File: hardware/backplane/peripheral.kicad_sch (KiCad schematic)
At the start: 1 part

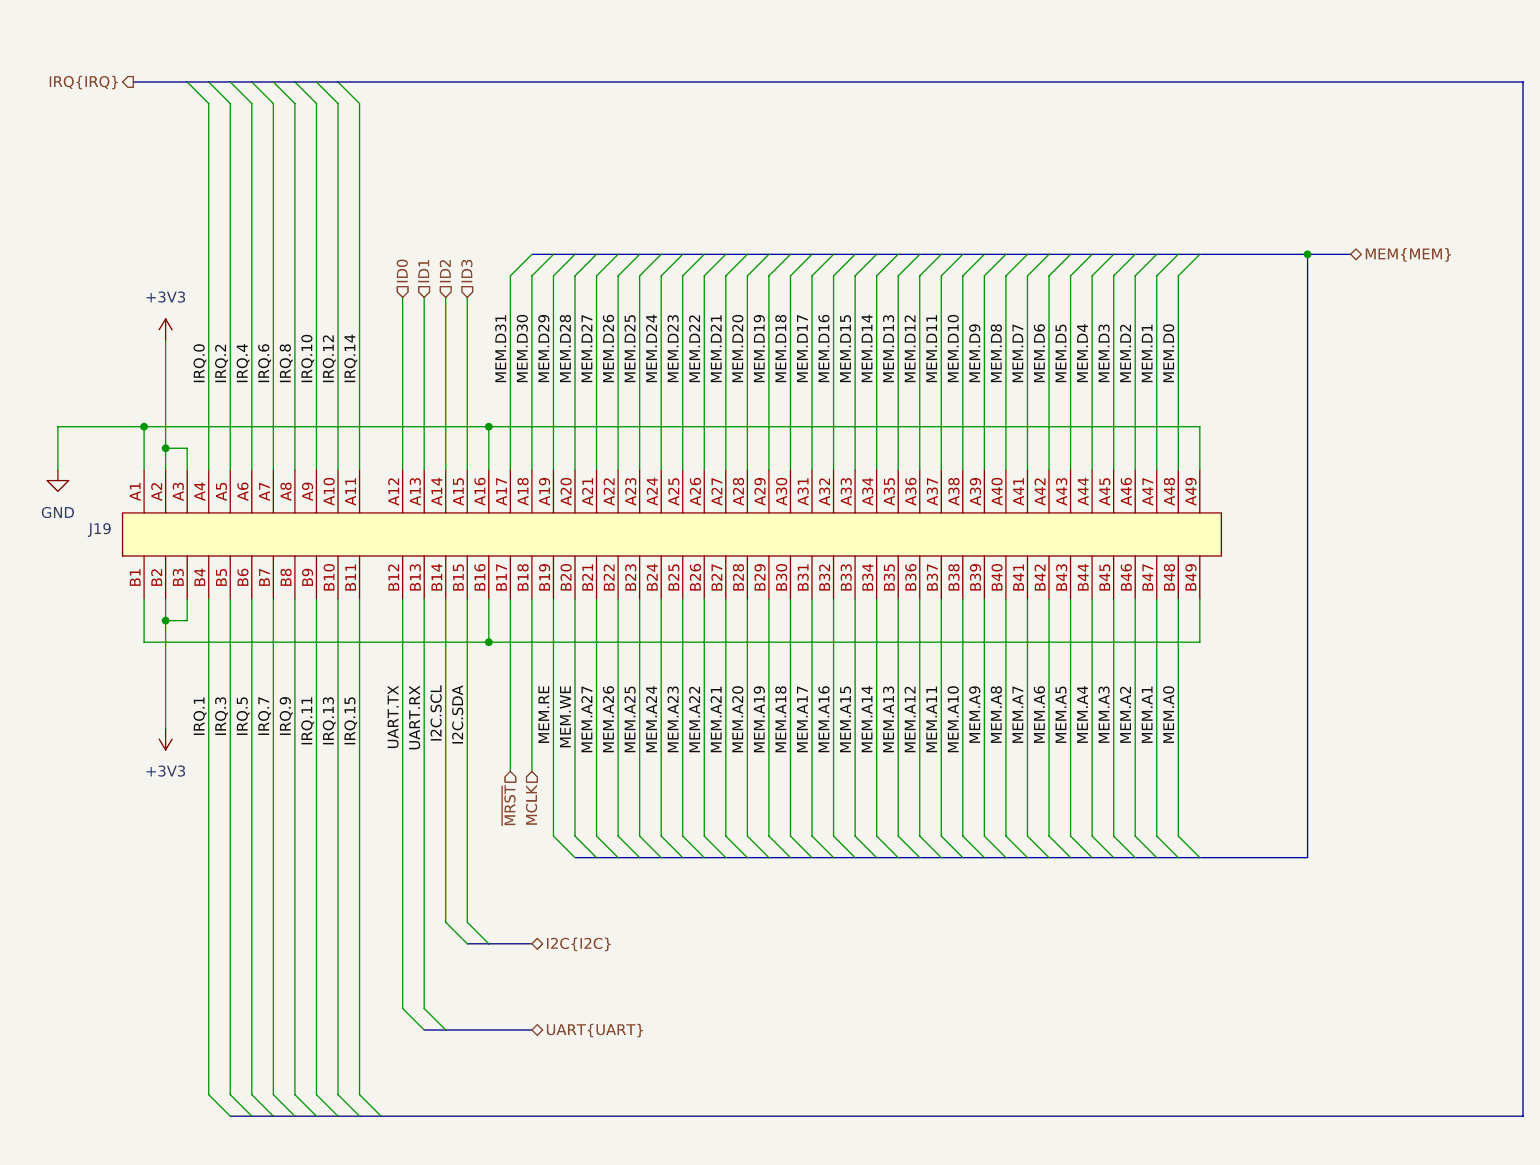
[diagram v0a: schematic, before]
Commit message: feat: Re-add peripheral MCLK, add to memory lines (#3)
Need MCLK to maintain peripheral synchronization.  Add missing memory
access size and latch lines.
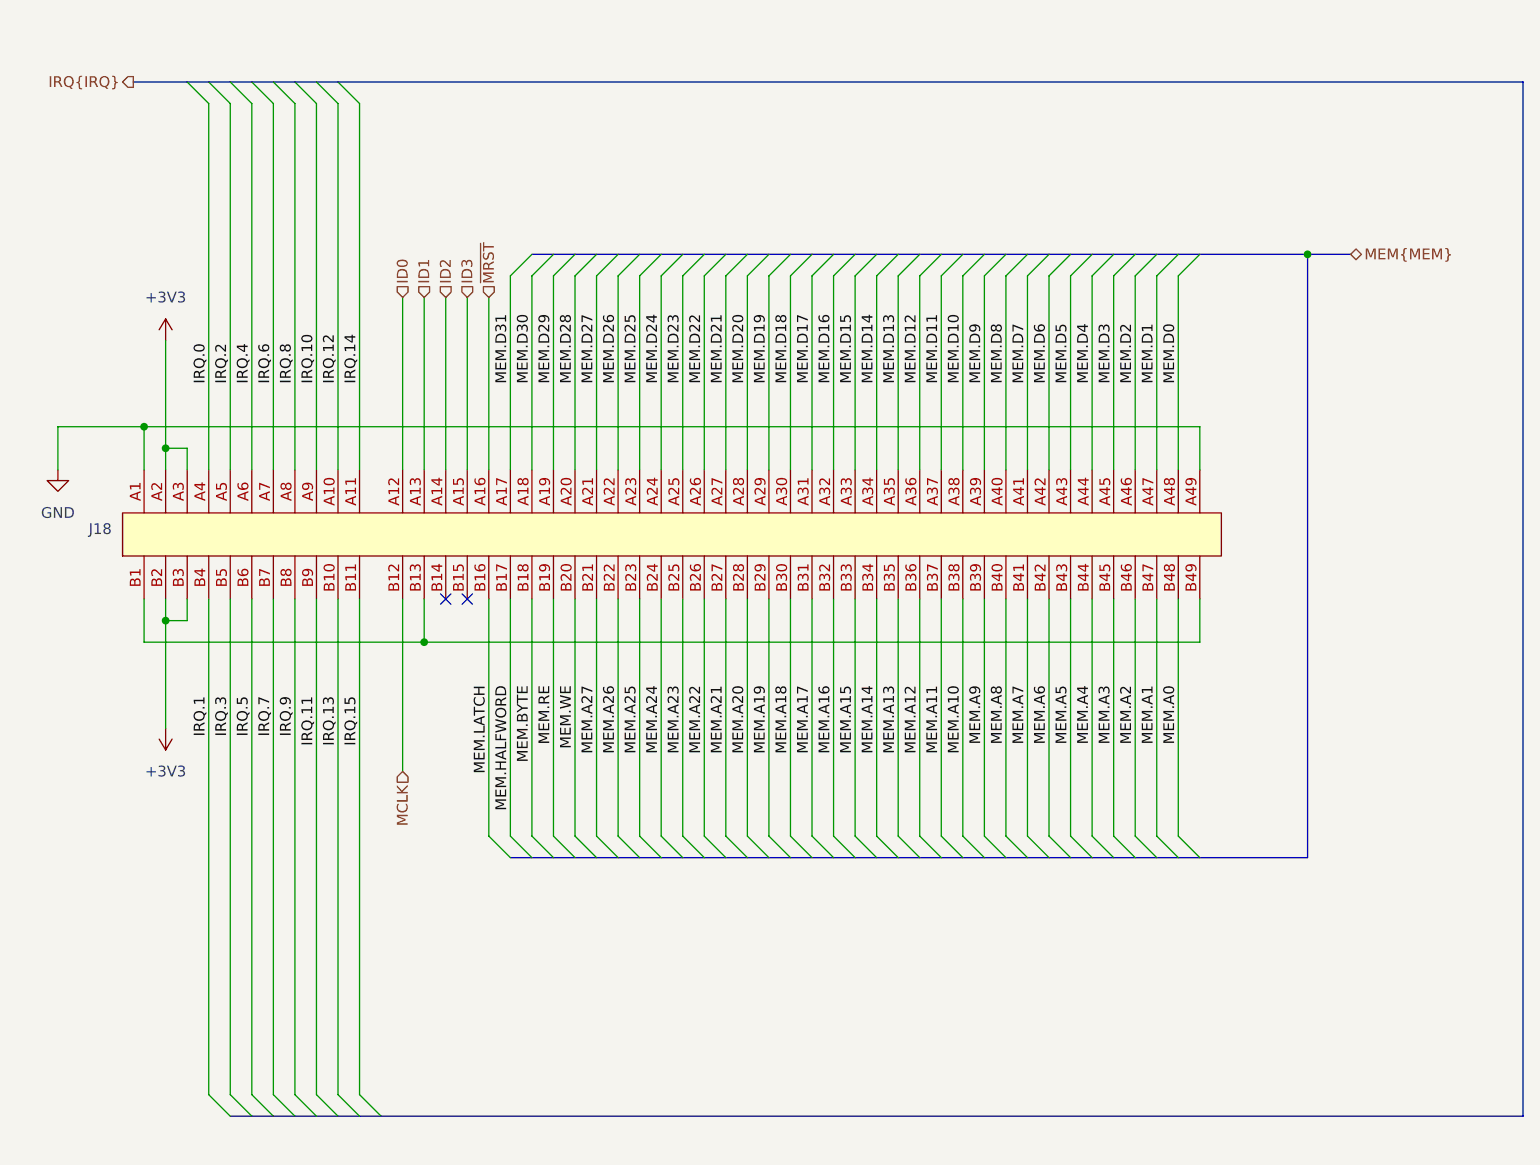
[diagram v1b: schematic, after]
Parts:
- renumbered J19 to J18
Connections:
- net UART.RX is gone; now on an unnamed net: J18.B13
- net UART.TX is gone; now on net MCLK: J18.B12
- net GND: no longer J18.A16
- net MCLK: no longer J18.B18
- net ~{MRST}: now also J18.A16; no longer J18.B17
- net at J18.B1, J18.B49: no longer J18.B16
- net I2C.SCL: no longer names the net of J18.B14
- net I2C.SDA: no longer names the net of J18.B15
- new net MEM.BYTE: J18.B18
- new net MEM.HALFWORD: J18.B17
- new net MEM.LATCH: J18.B16
- no-connect marks 0 -> 2

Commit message: feat: Assign footprints, add testpoints
 * Verify all footprints are assigned.
 * Create testpoints for key signals.
 * Reorganize component libraries.
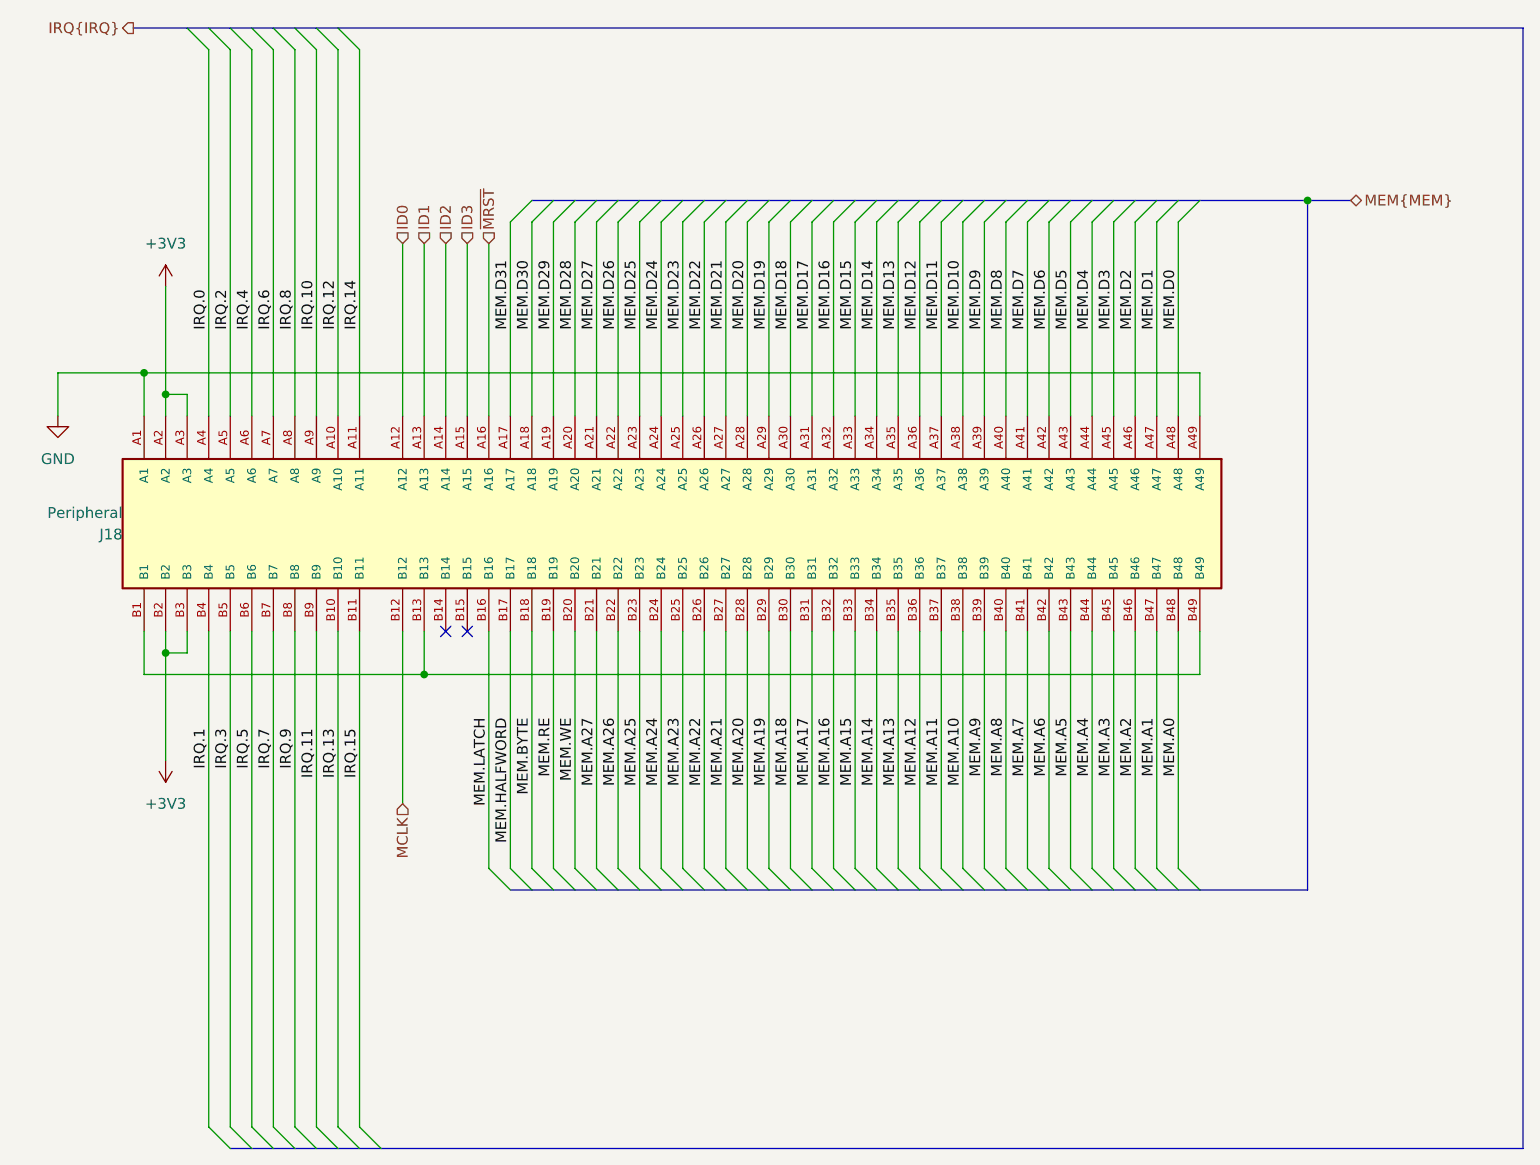
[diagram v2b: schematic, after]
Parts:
- removed J18: ~, symbol Connector_PCIe:PCIe_x8
- added J18: Peripheral, 10018783_10202TLF:AMPHENOL_10018783-10202TLF, symbol 10018783-10202TLF:10018783-10202TLF
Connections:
- net +3V3: now also J18.A2, J18.A3, J18.B2, J18.B3
- net GND: now also J18.A1, J18.A49
- net ID0: now also J18.A12
- net ID1: now also J18.A13
- net ID2: now also J18.A14
- net ID3: now also J18.A15
- net IRQ.0: now also J18.A4
- net IRQ.1: now also J18.B4
- net IRQ.10: now also J18.A9
- net IRQ.11: now also J18.B9
- net IRQ.12: now also J18.A10
- net IRQ.13: now also J18.B10
- net IRQ.14: now also J18.A11
- net IRQ.15: now also J18.B11
- net IRQ.2: now also J18.A5
- net IRQ.3: now also J18.B5
- net IRQ.4: now also J18.A6
- net IRQ.5: now also J18.B6
- net IRQ.6: now also J18.A7
- net IRQ.7: now also J18.B7
- net IRQ.8: now also J18.A8
- net IRQ.9: now also J18.B8
- net MCLK: now also J18.B12
- net MEM.A0: now also J18.B48
- net MEM.A1: now also J18.B47
- net MEM.A10: now also J18.B38
- net MEM.A11: now also J18.B37
- net MEM.A12: now also J18.B36
- net MEM.A13: now also J18.B35
- net MEM.A14: now also J18.B34
- net MEM.A15: now also J18.B33
- net MEM.A16: now also J18.B32
- net MEM.A17: now also J18.B31
- net MEM.A18: now also J18.B30
- net MEM.A19: now also J18.B29
- net MEM.A2: now also J18.B46
- net MEM.A20: now also J18.B28
- net MEM.A21: now also J18.B27
- net MEM.A22: now also J18.B26
- net MEM.A23: now also J18.B25
- net MEM.A24: now also J18.B24
- net MEM.A25: now also J18.B23
- net MEM.A26: now also J18.B22
- net MEM.A27: now also J18.B21
- net MEM.A3: now also J18.B45
- net MEM.A4: now also J18.B44
- net MEM.A5: now also J18.B43
- net MEM.A6: now also J18.B42
- net MEM.A7: now also J18.B41
- net MEM.A8: now also J18.B40
- net MEM.A9: now also J18.B39
- net MEM.BYTE: now also J18.B18
- net MEM.D0: now also J18.A48
- net MEM.D1: now also J18.A47
- net MEM.D10: now also J18.A38
- net MEM.D11: now also J18.A37
- net MEM.D12: now also J18.A36
- net MEM.D13: now also J18.A35
- net MEM.D14: now also J18.A34
- net MEM.D15: now also J18.A33
- net MEM.D16: now also J18.A32
- net MEM.D17: now also J18.A31
- net MEM.D18: now also J18.A30
- net MEM.D19: now also J18.A29
- net MEM.D2: now also J18.A46
- net MEM.D20: now also J18.A28
- net MEM.D21: now also J18.A27
- net MEM.D22: now also J18.A26
- net MEM.D23: now also J18.A25
- net MEM.D24: now also J18.A24
- net MEM.D25: now also J18.A23
- net MEM.D26: now also J18.A22
- net MEM.D27: now also J18.A21
- net MEM.D28: now also J18.A20
- net MEM.D29: now also J18.A19
- net MEM.D3: now also J18.A45
- net MEM.D30: now also J18.A18
- net MEM.D31: now also J18.A17
- net MEM.D4: now also J18.A44
- net MEM.D5: now also J18.A43
- net MEM.D6: now also J18.A42
- net MEM.D7: now also J18.A41
- net MEM.D8: now also J18.A40
- net MEM.D9: now also J18.A39
- net MEM.HALFWORD: now also J18.B17
- net MEM.LATCH: now also J18.B16
- net MEM.RE: now also J18.B19
- net MEM.WE: now also J18.B20
- net ~{MRST}: now also J18.A16
- new net: J18.B1, J18.B13, J18.B49

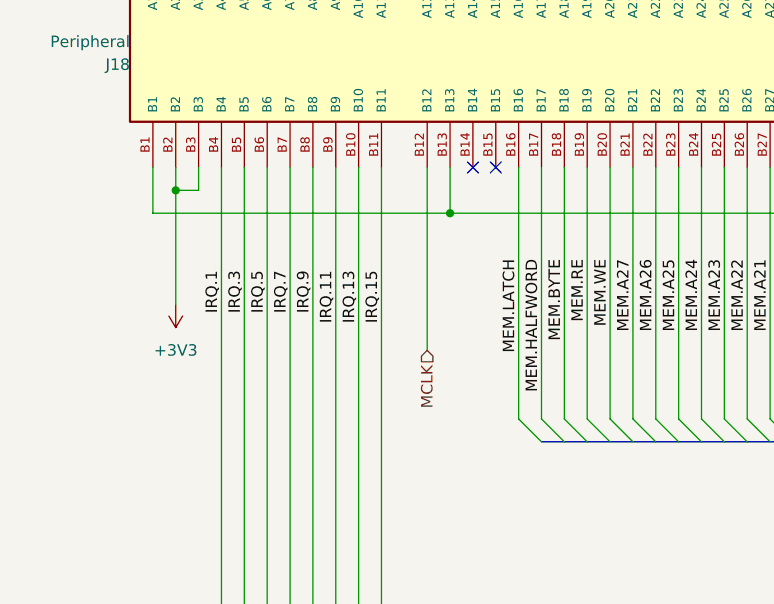
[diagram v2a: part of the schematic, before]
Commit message: feat: Apply bus arch changes to backplane schematic
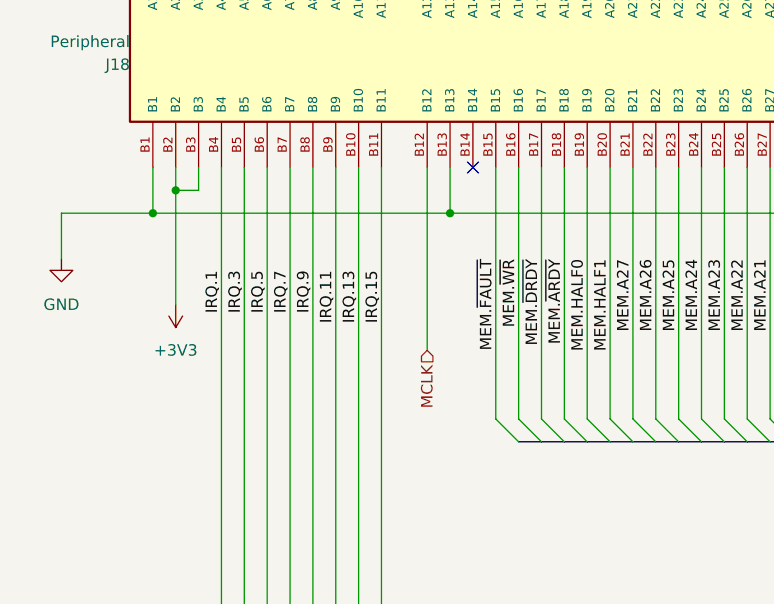
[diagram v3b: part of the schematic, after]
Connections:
- net GND: now also J18.B1, J18.B13, J18.B49
- net MEM.~{FAULT}: now reaches J18.B15
- net MEM.BYTE renamed MEM.~{ARDY}
- net MEM.HALFWORD renamed MEM.~{DRDY}
- net MEM.LATCH renamed MEM.~{WR}
- net MEM.RE renamed MEM.HALF0
- net MEM.WE renamed MEM.HALF1
- no-connect marks 2 -> 1
